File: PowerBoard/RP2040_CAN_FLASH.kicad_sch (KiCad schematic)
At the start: 60 parts, among them J1 B3B-XH-A_LF__SN_, J2 USB4145-03-0170-C_REVA2, J5 Conn_02x10_Counter_Clockwise, Q1 BSS138, Q4 BSS138, U1 RPI2040, U10 PTS647SM38SMTR2LFS, U5 W25Q128JVS, U7 MCP2515-xST, U8 MCP2551-I-SN, U9 PTS647SM38SMTR2LFS, Y1 ABM3-12.000MHZ-D2Y-T, Y2 ABM3-8.000MHZ-D2Y-T

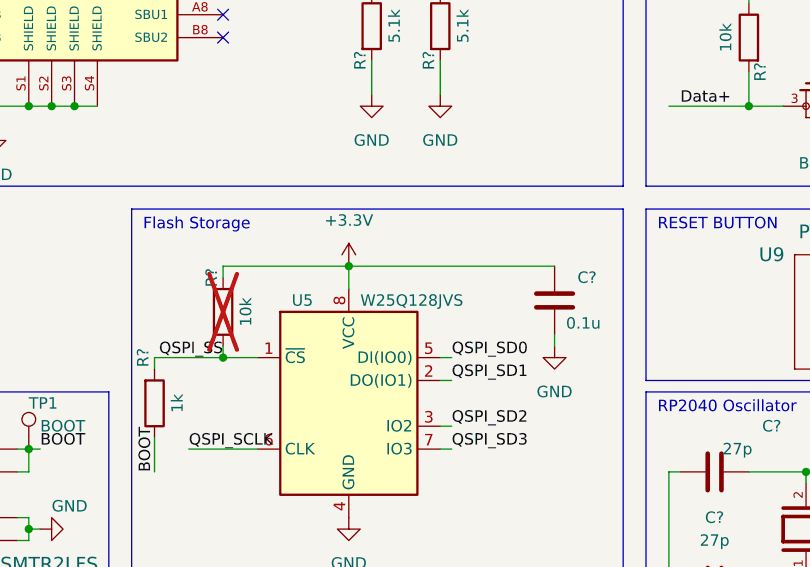
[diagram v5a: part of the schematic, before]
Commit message: updated layout for design review
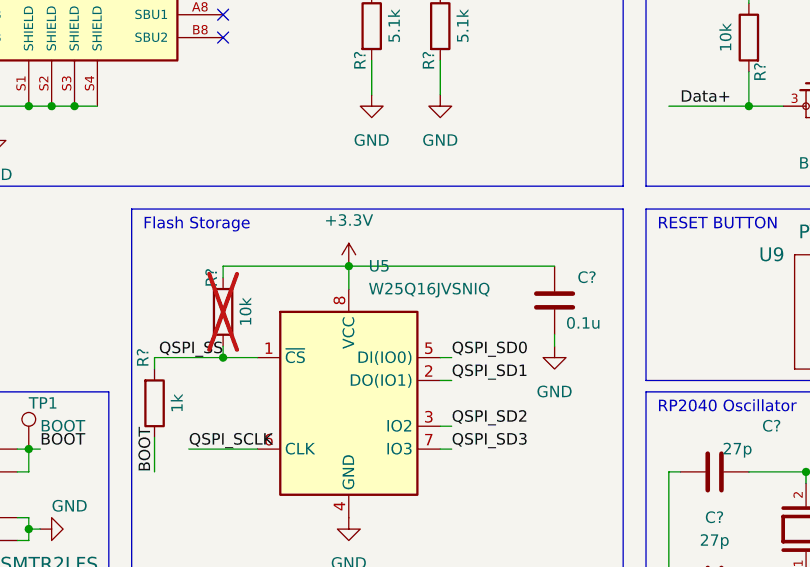
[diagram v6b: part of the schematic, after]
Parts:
- U5: value W25Q128JVS -> W25Q16JVSNIQ; JLC SOIC-8-208mil -> (none); LCSC C97521 -> (none)
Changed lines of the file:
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@@
-    )
-  )
-  (symbol (lib_id "bots:W25Q16JVSNIQ") (at 69.85 97.79 0) (unit 1)
-    (in_bom yes) (on_board yes) (dnp no)
-    (property "Reference" "U5" (at 63.5 86.36 0)
-      (effects (font (size 1.27 1.27)) (justify left))
-    )
-    (property "Value" "W25Q128JVS" (at 71.12 86.36 0)
-      (effects (font (size 1.27 1.27)) (justify left))
-    )
-    (property "Footprint" "bots:SOIC-8_3.9x4.9mm_P1.27mm" (at 69.85 97.79 0)
-      (effects (font (size 1.27 1.27)) hide)
-    )
-    (property "Datasheet" "http://www.winbond.com/resource-files/w25q128jv_dtr%20revc%2003272018%20plus.pdf" (at 69.85 97.79 0)
-      (effects (font (size 1.27 1.27)) hide)
-    )
-    (property "MPN" "W25Q128JVSIQ" (at 69.85 97.79 0)
-      (effects (font (size 1.27 1.27)) hide)
-    )
-    (property "Manufacturer" "Winbond Elec" (at 69.85 97.79 0)
-      (effects (font (size 1.27 1.27)) hide)
-    )
-    (property "Price" "0.5635" (at 69.85 97.79 0)
-      (effects (font (size 1.27 1.27)) hide)
-    )
-    (property "JLC" "SOIC-8-208mil" (at 69.85 97.79 0)
-      (effects (font (size 1.27 1.27)) hide)
-    )
-    (property "LCSC" "C97521" (at 69.85 97.79 0)
-      (effects (font (size 1.27 1.27)) hide)
-    )
-    (property "Description" "FLASH - NOR Memory IC 16Mbit SPI - Quad I/O 133 MHz 8-SOIC" (at 69.85 97.79 0)
-      (effects (font (size 1.27 1.27)) hide)
-    )
-    (pin "1")
-    (pin "2")
-    (pin "3")
-    (pin "4")
-    (pin "5")
-    (pin "6")
-    (pin "7")
-    (pin "8")
-    (instances
-      (project "POWER_BOARD"
-        (path "/1a9ce3e8-a091-496c-9c5f-e7b2eb60e275/44109b35-87db-4b37-b749-86ba1243ffef"
-          (reference "U5") (unit 1)
-        )
-        (path "/1a9ce3e8-a091-496c-9c5f-e7b2eb60e275/aa68550e-c35d-4fef-b4e5-f1eb6225215f"
-          (reference "U11") (unit 1)
-        )
-      )
     )
   )
@@
         )
       )
+    )
+  )
+  (symbol (lib_id "bots:W25Q16JVSNIQ") (at 69.85 97.79 0) (unit 1)
+    (in_bom yes) (on_board yes) (dnp no) (fields_autoplaced)
+    (property "Reference" "U5" (at 72.0441 82.55 0)
+      (effects (font (size 1.27 1.27)) (justify left))
+    )
+    (property "Value" "W25Q16JVSNIQ" (at 72.0441 85.09 0)
+      (effects (font (size 1.27 1.27)) (justify left))
+    )
+    (property "Footprint" "bots:SOIC-8_3.9x4.9mm_P1.27mm" (at 69.85 97.79 0)
+      (effects (font (size 1.27 1.27)) hide)
+    )
+    (property "Datasheet" "http://www.winbond.com/resource-files/w25q128jv_dtr%20revc%2003272018%20plus.pdf" (at 69.85 97.79 0)
+      (effects (font (size 1.27 1.27)) hide)
+    )
+    (property "MPN" "W25Q128JVSIQ" (at 69.85 97.79 0)
+      (effects (font (size 1.27 1.27)) hide)
+    )
+    (property "Manufacturer" "Winbond Elec" (at 69.85 97.79 0)
+      (effects (font (size 1.27 1.27)) hide)
+    )
+    (property "Price" "0.5635" (at 69.85 97.79 0)
+      (effects (font (size 1.27 1.27)) hide)
+    )
+    (property "JLC" "" (at 69.85 97.79 0)
+      (effects (font (size 1.27 1.27)) hide)
+    )
+    (property "LCSC" "" (at 69.85 97.79 0)
+      (effects (font (size 1.27 1.27)) hide)
+    )
+    (property "Description" "FLASH - NOR Memory IC 16Mbit SPI - Quad I/O 133 MHz 8-SOIC" (at 69.85 97.79 0)
+      (effects (font (size 1.27 1.27)) hide)
+    )
+    (pin "1")
+    (pin "2")
+    (pin "3")
+    (pin "4")
+    (pin "5")
+    (pin "6")
+    (pin "7")
+    (pin "8")
+    (instances
+      (project "POWER_BOARD"
+        (path "/1a9ce3e8-a091-496c-9c5f-e7b2eb60e275/44109b35-87db-4b37-b749-86ba1243ffef"
+          (reference "U5") (unit 1)
+        )
+      )

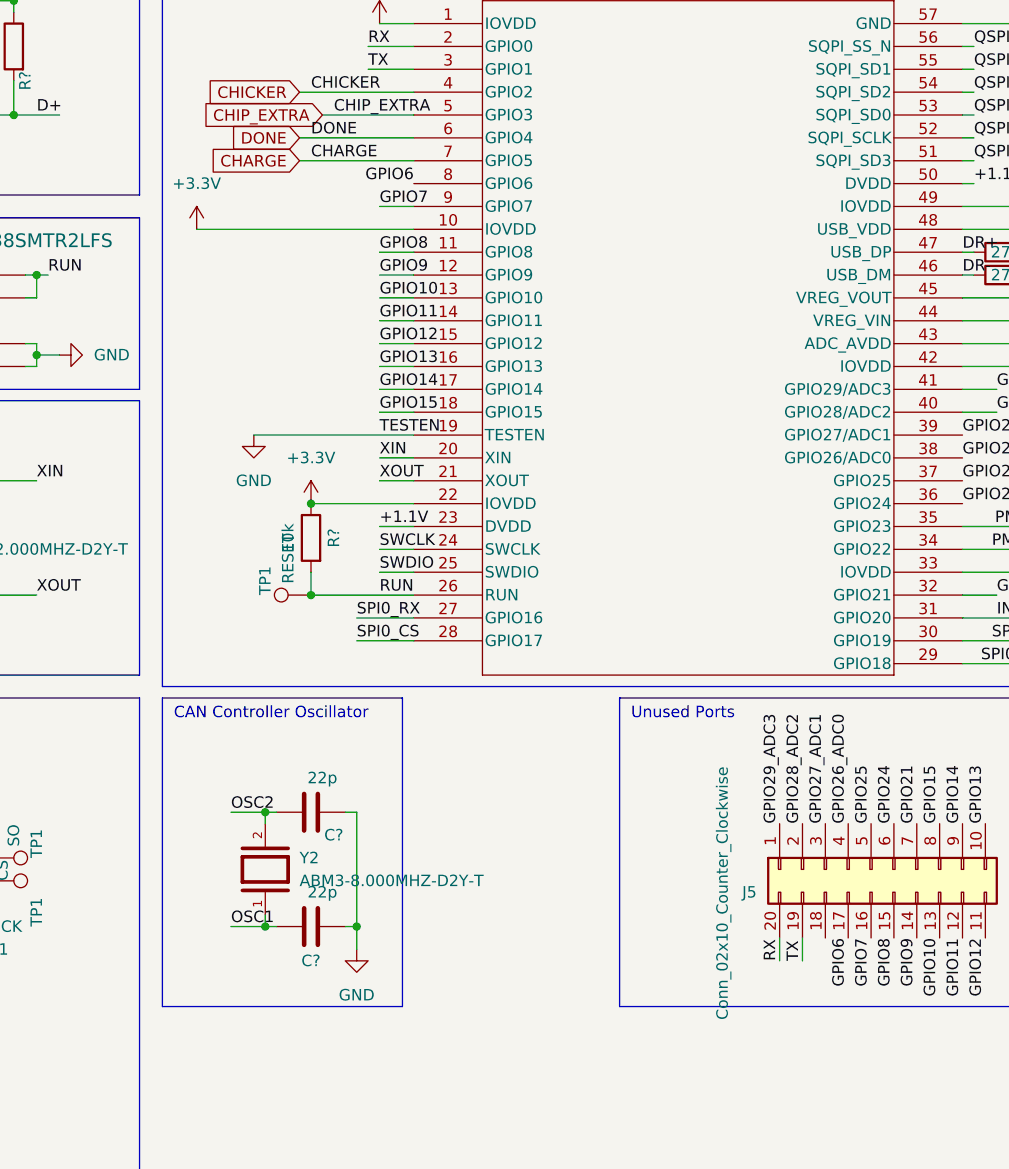
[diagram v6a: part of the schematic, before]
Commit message: updated fuse, pillars, caps
- Added 10A fuse to VCC pillar
- Added CANL pillar next to CANH (and old CANL pillar is NC)
- Adjusted CAPS left and right by 1mm to add space for the board
- Added another LED wired to the RP2040 for CAN status
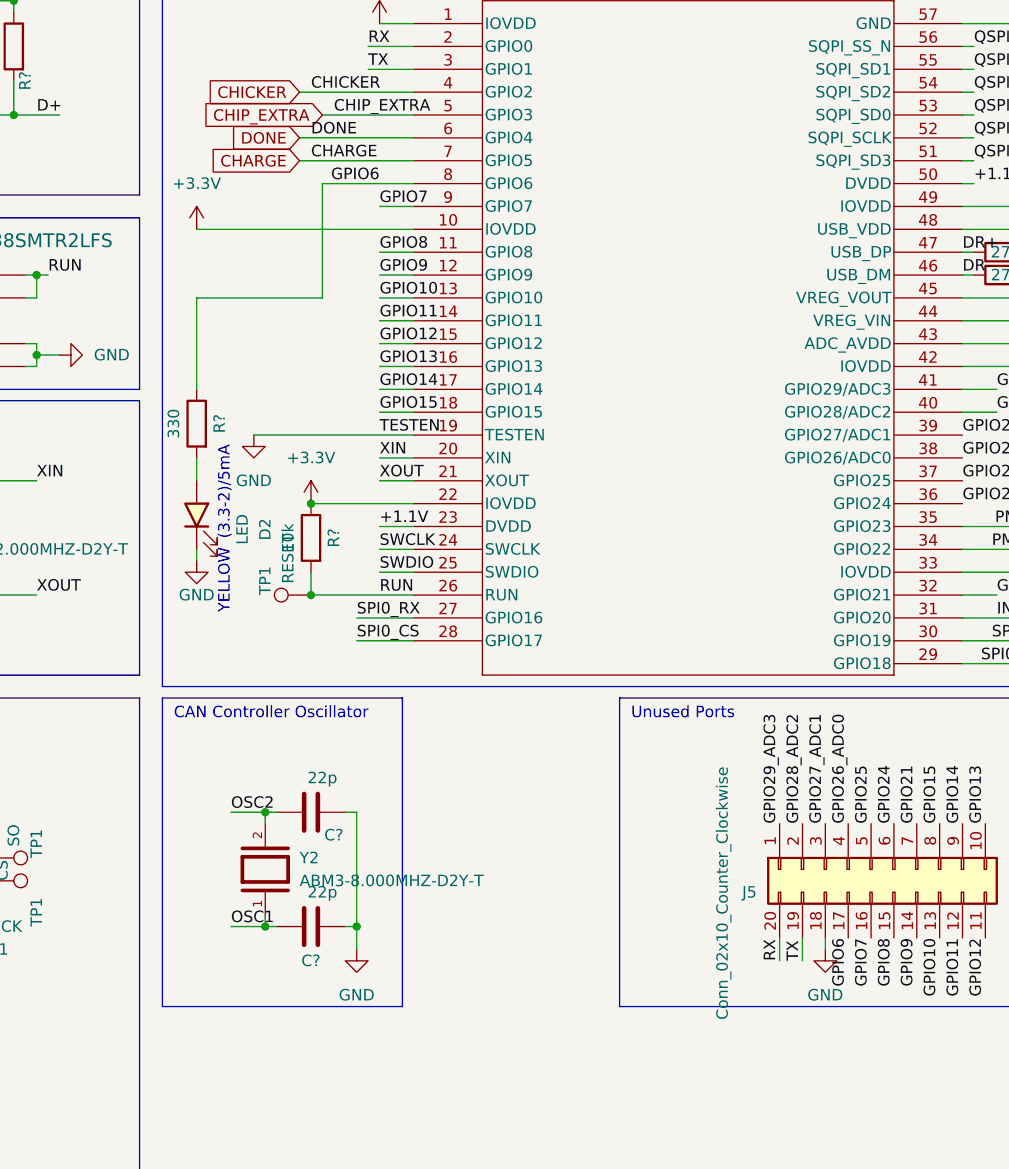
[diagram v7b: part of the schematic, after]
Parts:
- added D2: LED, bots:LED_0603_1608Metric, symbol bots:LED_yellow
- added R?: 330, bots:R_0603_1608Metric, symbol bots:R_330R
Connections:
- net GND: now also J5.18 (Pin_18), D2.1 (K)
- net GPIO6: now also R?.1
- new net: D2.2 (A), R?.2
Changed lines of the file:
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@@
     (stroke (width 0) (type default))
   )
+  (wire (pts (xy 223.52 156.21) (xy 223.52 157.48))
+    (stroke (width 0) (type default))
+  )
   (wire (pts (xy 176.53 24.13) (xy 176.53 25.4))
     (stroke (width 0) (type default))
@@
     (stroke (width 0) (type default))
   )
+  (wire (pts (xy 167.64 72.39) (xy 177.8 72.39))
+    (stroke (width 0) (type default))
+  )
   (wire (pts (xy 55.88 35.56) (xy 58.42 35.56))
     (stroke (width 0) (type default))
@@
     (stroke (width 0) (type default))
   )
+  (wire (pts (xy 153.67 85.09) (xy 153.67 95.25))
+    (stroke (width 0) (type default))
+  )
   (wire (pts (xy 34.29 111.76) (xy 34.29 110.49))
     (stroke (width 0) (type default))
@@
     (stroke (width 0) (type default))
   )
+  (wire (pts (xy 153.67 113.03) (xy 153.67 114.3))
+    (stroke (width 0) (type default))
+  )
   (wire (pts (xy 114.3 34.29) (xy 114.3 38.1))
     (stroke (width 0) (type default))
@@
     (stroke (width 0) (type default))
   )
-  (wire (pts (xy 173.99 92.71) (xy 177.8 92.71))
-    (stroke (width 0) (type default))
-  )
   (wire (pts (xy 238.76 69.85) (xy 240.03 69.85))
     (stroke (width 0) (type default))
@@
     (stroke (width 0) (type default))
   )
+  (wire (pts (xy 167.64 85.09) (xy 167.64 72.39))
+    (stroke (width 0) (type default))
+  )
   (wire (pts (xy 238.76 118.11) (xy 242.57 118.11))
     (stroke (width 0) (type default))
@@
     (stroke (width 0) (type default))
   )
+  (wire (pts (xy 153.67 102.87) (xy 153.67 105.41))
+    (stroke (width 0) (type default))
+  )
   (wire (pts (xy 69.85 82.55) (xy 92.71 82.55))
     (stroke (width 0) (type default))
@@
     (stroke (width 0) (type default))
   )
+  (wire (pts (xy 153.67 85.09) (xy 167.64 85.09))
+    (stroke (width 0) (type default))
+  )
   (wire (pts (xy 238.76 74.93) (xy 247.65 74.93))
     (stroke (width 0) (type default))
   )
+  (wire (pts (xy 173.99 92.71) (xy 177.8 92.71))
+    (stroke (width 0) (type default))
+  )
   (wire (pts (xy 251.46 149.86) (xy 251.46 151.13))
     (stroke (width 0) (type default))
@@
     (effects (font (size 1.27 1.27)) (justify left bottom))
   )
+  (text "(3.3-2)/5mA" (at 157.48 101.6 90)
+    (effects (font (size 1.27 1.27) (color 0 4 0 1)) (justify right bottom))
+  )
   (text "SWD Connector" (at 247.65 132.08 0)
     (effects (font (size 1.27 1.27)) (justify left bottom))
   )
+  (text "YELLOW" (at 157.48 113.03 90)
+    (effects (font (size 1.27 1.27) (color 251 249 0 1)) (justify right bottom))
+  )
   (text "Decoupling Caps" (at 151.13 17.78 0)
     (effects (font (size 1.27 1.27)) (justify left bottom))
@@
     (effects (font (size 1.27 1.27)) (justify left bottom))
   )
-  (label "GPIO6" (at 177.8 72.39 180) (fields_autoplaced)
+  (label "GPIO6" (at 173.99 72.39 180) (fields_autoplaced)
     (effects (font (size 1.27 1.27)) (justify right bottom))
   )
@@
     )
   )
+  (symbol (lib_id "bots:R_330R") (at 153.67 99.06 0) (mirror y) (unit 1)
+    (in_bom yes) (on_board yes) (dnp no)
+    (property "Reference" "R?" (at 156.21 99.06 90)
+      (effects (font (size 1.27 1.27)))
+    )
+    (property "Value" "330" (at 151.13 99.06 90)
+      (effects (font (size 1.27 1.27)))
+    )
+    (property "Footprint" "bots:R_0603_1608Metric" (at 155.448 99.06 90)
+      (effects (font (size 1.27 1.27)) hide)
+    )
+    (property "Datasheet" "~" (at 153.67 99.06 0)
+      (effects (font (size 1.27 1.27)) hide)
+    )
+    (property "MPN" "0603WAF3300T5E" (at 153.67 99.06 0)
+      (effects (font (size 1.27 1.27)) hide)
+    )
+    (property "Manufacturer" "UNI-ROYAL(Uniroyal Elec)" (at 153.67 99.06 0)
+      (effects (font (size 1.27 1.27)) hide)
+    )
+    (property "Price" "0.0009" (at 153.67 99.06 0)
+      (effects (font (size 1.27 1.27)) hide)
+    )
+    (property "JLC" "0603" (at 153.67 99.06 0)
+      (effects (font (size 1.27 1.27)) hide)
+    )
+    (property "LCSC" "C23138" (at 153.67 99.06 0)
+      (effects (font (size 1.27 1.27)) hide)
+    )
+    (pin "1")
+    (pin "2")
+    (instances
+      (project "POWER_BOARD"
+        (path "/1a9ce3e8-a091-496c-9c5f-e7b2eb60e275"
+          (reference "R?") (unit 1)
+        )
+        (path "/1a9ce3e8-a091-496c-9c5f-e7b2eb60e275/44109b35-87db-4b37-b749-86ba1243ffef"
+          (reference "R45") (unit 1)
+        )
+        (path "/1a9ce3e8-a091-496c-9c5f-e7b2eb60e275/aa68550e-c35d-4fef-b4e5-f1eb6225215f"
+          (reference "R53") (unit 1)
+        )
+      )
+    )
+  )
   (symbol (lib_id "bots:R_10k") (at 133.35 30.48 0) (mirror y) (unit 1)
     (in_bom yes) (on_board yes) (dnp no)
@@
     )
   )
+  (symbol (lib_id "power:GND") (at 223.52 157.48 0) (unit 1)
+    (in_bom yes) (on_board yes) (dnp no) (fields_autoplaced)
+    (property "Reference" "#PWR?" (at 223.52 163.83 0)
+      (effects (font (size 1.27 1.27)) hide)
+    )
+    (property "Value" "GND" (at 223.52 162.56 0)
+      (effects (font (size 1.27 1.27)))
+    )
+    (property "Footprint" "" (at 223.52 157.48 0)
+      (effects (font (size 1.27 1.27)) hide)
+    )
+    (property "Datasheet" "" (at 223.52 157.48 0)
+      (effects (font (size 1.27 1.27)) hide)
+    )
+    (pin "1")
+    (instances
+      (project "POWER_BOARD"
+        (path "/1a9ce3e8-a091-496c-9c5f-e7b2eb60e275"
+          (reference "#PWR?") (unit 1)
+        )
+        (path "/1a9ce3e8-a091-496c-9c5f-e7b2eb60e275/44109b35-87db-4b37-b749-86ba1243ffef"
+          (reference "#PWR075") (unit 1)
+        )
+        (path "/1a9ce3e8-a091-496c-9c5f-e7b2eb60e275/aa68550e-c35d-4fef-b4e5-f1eb6225215f"
+          (reference "#PWR090") (unit 1)
+        )
+      )
+    )
+  )
   (symbol (lib_id "power:+3.3V") (at 153.67 77.47 0) (unit 1)
     (in_bom yes) (on_board yes) (dnp no) (fields_autoplaced)
@@
         )
       )
+    )
+  )
+  (symbol (lib_id "bots:LED_yellow") (at 153.67 109.22 90) (unit 1)
+    (in_bom yes) (on_board yes) (dnp no) (fields_autoplaced)
+    (property "Reference" "D2" (at 161.29 110.8075 0)
+      (effects (font (size 1.27 1.27)))
+    )
+    (property "Value" "LED" (at 158.75 110.8075 0)
+      (effects (font (size 1.27 1.27)))
+    )
+    (property "Footprint" "bots:LED_0603_1608Metric" (at 153.67 109.22 0)
+      (effects (font (size 1.27 1.27)) hide)
+    )
+    (property "Datasheet" "~" (at 153.67 109.22 0)
+      (effects (font (size 1.27 1.27)) hide)
+    )
+    (property "MPN" "19-21UYC/S530-A4/TR8" (at 153.67 109.22 0)
+      (effects (font (size 1.27 1.27)) hide)
+    )
+    (property "Manufacturer" "Everlight Elec" (at 153.67 109.22 0)
+      (effects (font (size 1.27 1.27)) hide)
+    )
+    (property "Price" "0.0404" (at 153.67 109.22 0)
+      (effects (font (size 1.27 1.27)) hide)
+    )
+    (property "JLC" "0603" (at 153.67 109.22 0)
+      (effects (font (size 1.27 1.27)) hide)
+    )
+    (property "LCSC" "C409441" (at 153.67 109.22 0)
+      (effects (font (size 1.27 1.27)) hide)
+    )
+    (pin "1")
+    (pin "2")
+    (instances
+      (project "POWER_BOARD"
+        (path "/1a9ce3e8-a091-496c-9c5f-e7b2eb60e275"
+          (reference "D2") (unit 1)
+        )
+        (path "/1a9ce3e8-a091-496c-9c5f-e7b2eb60e275/aa68550e-c35d-4fef-b4e5-f1eb6225215f"
+          (reference "D4") (unit 1)
+        )
+        (path "/1a9ce3e8-a091-496c-9c5f-e7b2eb60e275/44109b35-87db-4b37-b749-86ba1243ffef"
+          (reference "D13") (unit 1)
+        )
+      )
+    )
+  )
+  (symbol (lib_id "power:GND") (at 153.67 114.3 0) (unit 1)
+    (in_bom yes) (on_board yes) (dnp no)
+    (property "Reference" "#PWR07" (at 153.67 120.65 0)
+      (effects (font (size 1.27 1.27)) hide)
+    )
+    (property "Value" "GND" (at 153.67 118.11 0)
+      (effects (font (size 1.27 1.27)))
+    )
+    (property "Footprint" "" (at 153.67 114.3 0)
+      (effects (font (size 1.27 1.27)) hide)
+    )
+    (property "Datasheet" "" (at 153.67 114.3 0)
+      (effects (font (size 1.27 1.27)) hide)
+    )
+    (pin "1")
+    (instances
+      (project "POWER_BOARD"
+        (path "/1a9ce3e8-a091-496c-9c5f-e7b2eb60e275"
+          (reference "#PWR07") (unit 1)
+        )
+        (path "/1a9ce3e8-a091-496c-9c5f-e7b2eb60e275/aa68550e-c35d-4fef-b4e5-f1eb6225215f"
+          (reference "#PWR021") (unit 1)
+        )
+        (path "/1a9ce3e8-a091-496c-9c5f-e7b2eb60e275/44109b35-87db-4b37-b749-86ba1243ffef"
+          (reference "#PWR074") (unit 1)
+        )
+      )

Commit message: passed DRC check
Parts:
- Y2: footprint bots:445C25D12M00000 -> bots:ABM3; MANUFACTURER (none) -> Cardinal Components
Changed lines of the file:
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@@
       (effects (font (size 1.27 1.27)) (justify right))
     )
-    (property "Footprint" "bots:445C25D12M00000" (at 161.29 148.59 0)
+    (property "Footprint" "bots:ABM3" (at 161.29 148.59 0)
       (effects (font (size 1.27 1.27)) (justify bottom) hide)
     )
@@
       (effects (font (size 1.27 1.27)) hide)
     )
+    (property "MANUFACTURER" "Cardinal Components" (at 161.29 148.59 0)
+      (effects (font (size 1.27 1.27)) (justify bottom) hide)
+    )
     (pin "1")
